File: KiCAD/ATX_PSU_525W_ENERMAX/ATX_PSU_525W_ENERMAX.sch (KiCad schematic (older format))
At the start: 87 parts

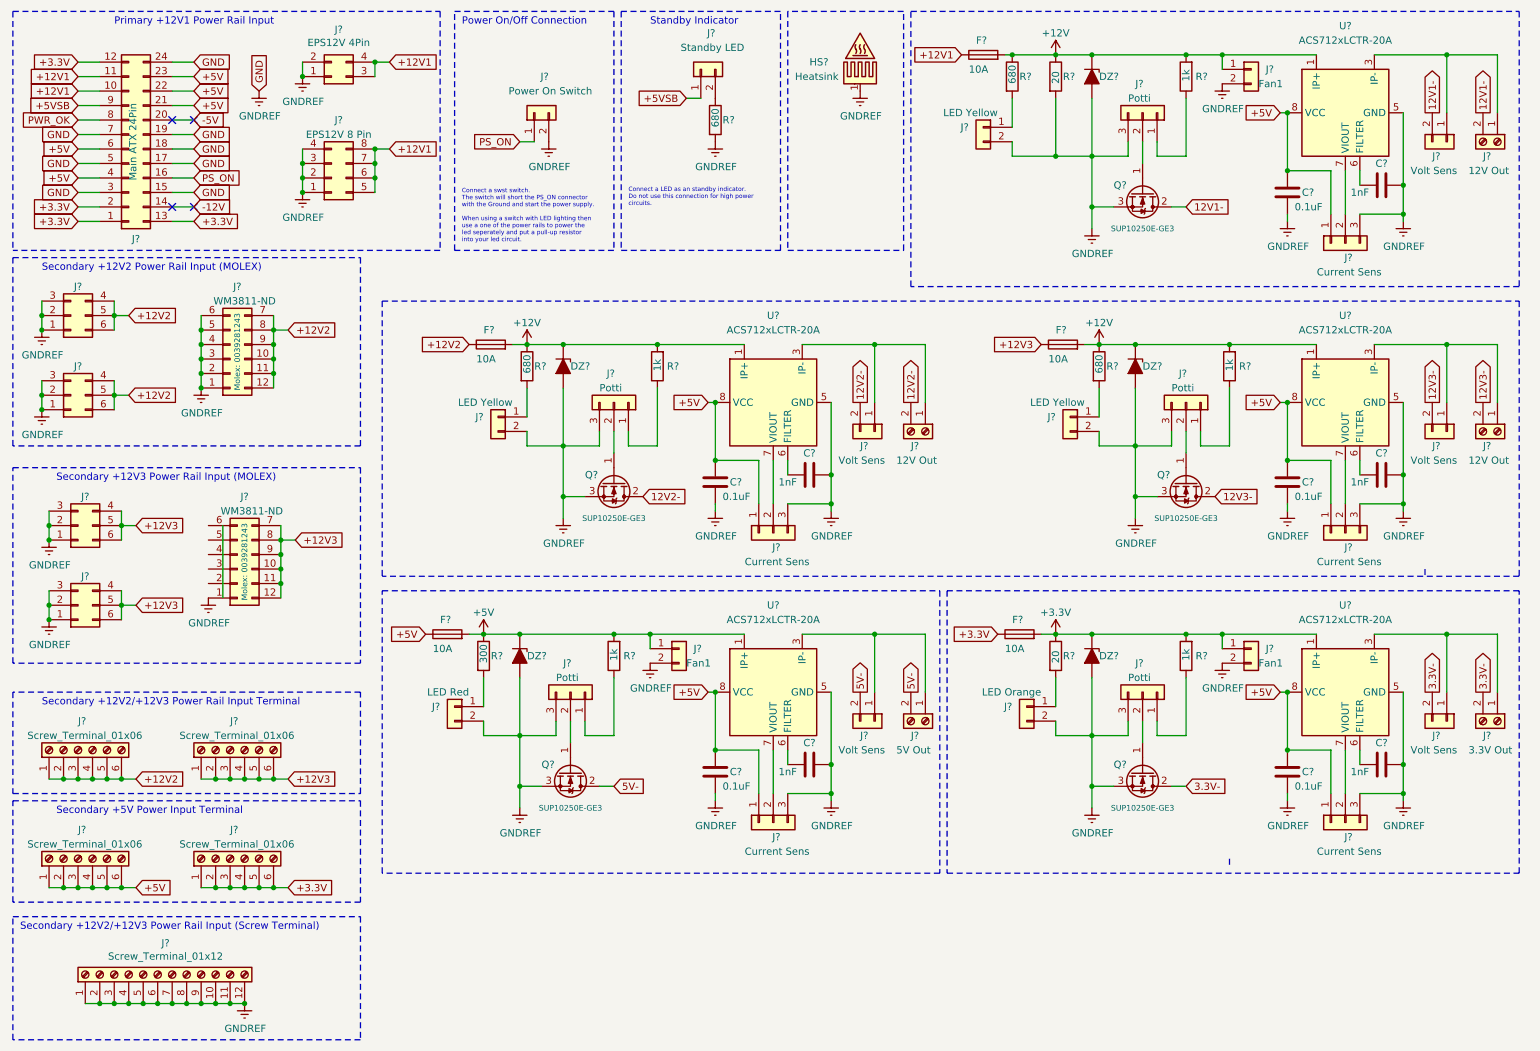
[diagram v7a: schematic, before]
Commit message: Annotated schematic symbols
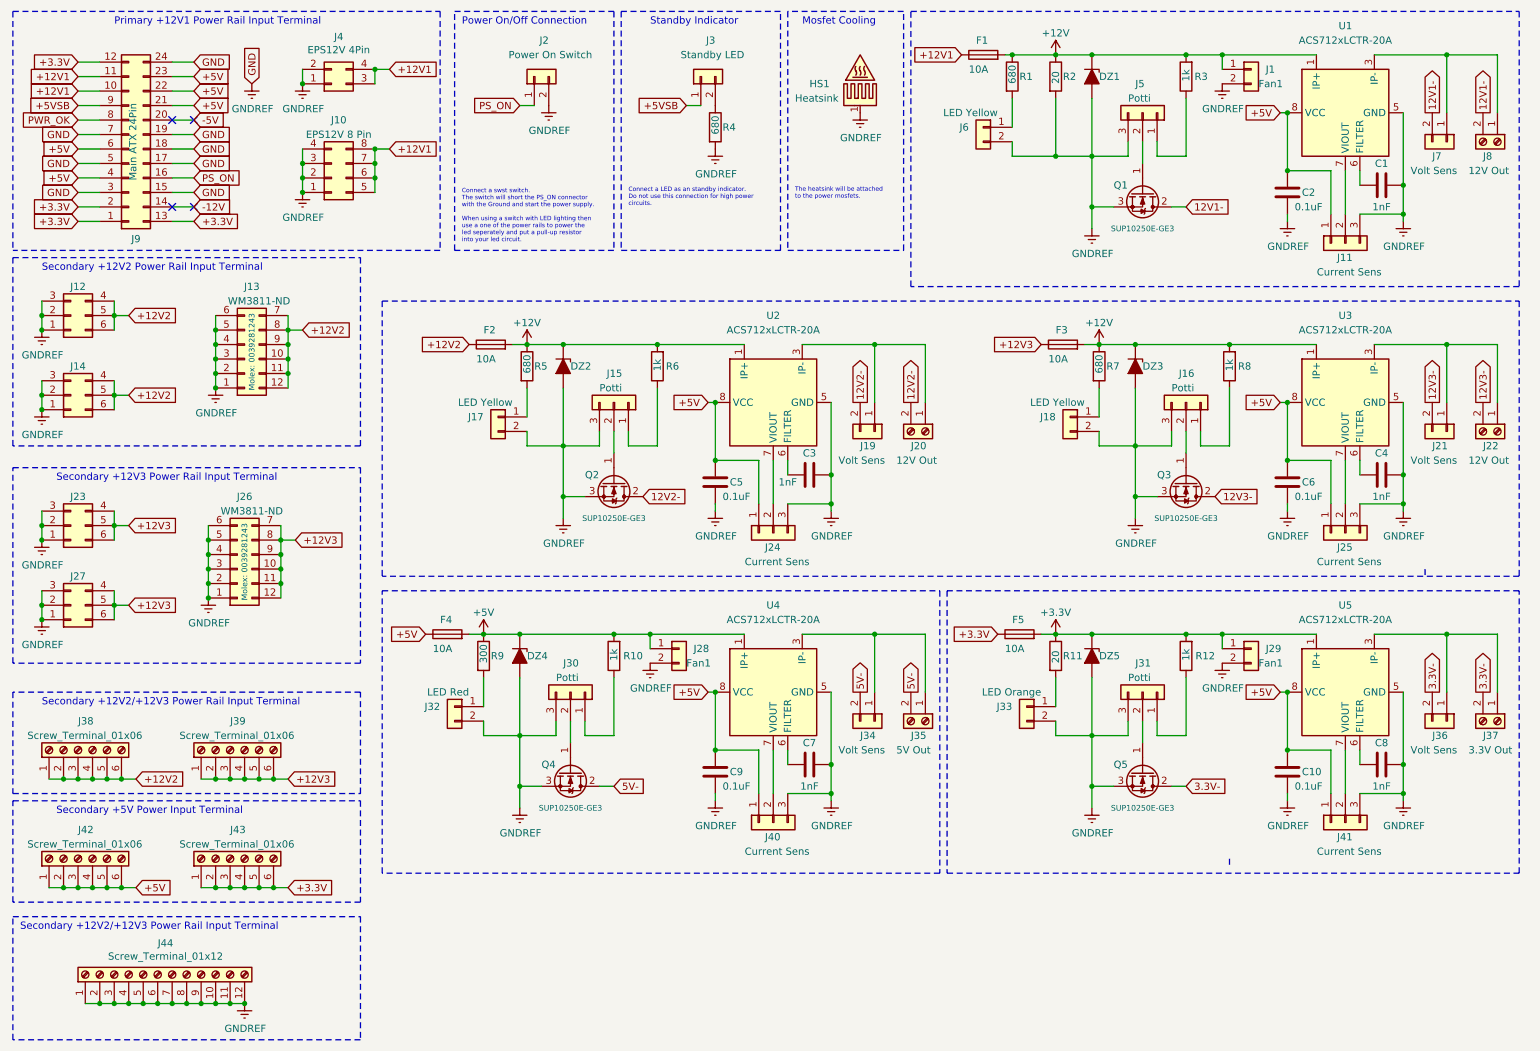
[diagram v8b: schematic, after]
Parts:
- gave numbers to parts that had none: 87
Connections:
- net GNDREF: now also J26.2 (Pin_2), J26.3 (Pin_3), J26.4 (Pin_4), J26.5 (Pin_5), J26.6 (Pin_6)
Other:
- note added: "Mosfet Cooling"
- note added: "Primary +12V1 Power Rail Input Terminal"
- note added: "Secondary +12V2 Power Rail Input Terminal"
- note added: "Secondary +12V3 Power Rail Input Terminal"
- note added: "The heatsink will be attached\nto the power mosfets."
- note removed: "Primary +12V1 Power Rail Input"
- note removed: "Secondary +12V2 Power Rail Input (MOLEX)"
- note removed: "Secondary +12V2/+12V3 Power Rail Input (Screw Terminal)"
- note removed: "Secondary +12V3 Power Rail Input (MOLEX)"
- moved on the sheet: HS1, J13, J2, J23, J27, J3, J4, R4
